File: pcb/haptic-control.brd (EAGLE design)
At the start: 40 x 160 mm, 148 parts, among them M1 SPH0641LM4H-1, P1 2P-PAD_1X3.5, P2 2P-PAD_1X3.5, P3 2P-PAD_1X3.5, P4 2P-PAD_1X3.5, U1 MIC23159, U10 DRV2605L, U11 DRV2605L, U12 MTCH6301, U2 BQ51050B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

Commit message: Nothing to do Needs revision
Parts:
- moved C52 31.9 mm to (14.2, 44.9), turned to 90 degrees
- moved R32 31.9 mm to (13.0, 44.9), turned to 270 degrees
- moved C51 27.0 mm to (9.70, 67.0)
- moved R30 27.0 mm to (9.70, 65.7)
- moved C56 22.4 mm to (30.1, 46.0), turned to 180 degrees
- moved R36 19.9 mm to (30.1, 47.2), turned to 0 degrees
- moved JP3 16.6 mm to (33.3, 42.4)
- moved JP1 16.5 mm to (37.0, 24.4), turned to 180 degrees
- moved JP2 14.5 mm to (37.0, 27.2), turned to 180 degrees
- moved C25 14.2 mm to (30.2, 42.4), turned to 90 degrees
- moved R20 13.4 mm to (31.5, 42.4), turned to 90 degrees
- moved C55 10.5 mm to (27.9, 63.8), turned to 180 degrees
- moved R34 8.29 mm to (27.9, 65.0), turned to 0 degrees
- moved C10 6.01 mm to (11.7, 35.3), turned to 270 degrees
- moved C32 4.32 mm to (26.1, 30.4)
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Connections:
- net FSR_CH_N renamed FSR_2
- removed net FSR_CH_P: C51.1, R29.1, R30.2, U5.39
- removed net FSR_VOL_N: C56.1, R35.2, R36.2, U5.37
- removed net FSR_VOL_P: C55.1, R33.2, R34.2, U5.40
- new net FSR_1: C51.1, R29.1, R30.2, U5.37
- new net FSR_3: C55.1, R33.2, R34.2, U5.39
- new net FSR_4: C56.1, R35.2, R36.2, U5.40
- net !QI_CHG: now also U5.19; no longer U5.18
- net 1V8_PG: now also U5.41; no longer U5.20
- net I2S_CLK: now also U5.31; no longer U5.30
- net I2S_DATIN: now also U5.30; no longer U5.29
- net LRA_EN: now also U5.14; no longer U5.6
- net MPU_INT: now also U5.32; no longer U5.28
- net QI_CTRL: now also U5.18; no longer U5.19
- net SCL: no longer R23.1
- net SDA: now also R23.1
- net TC_!RESET: now also U5.28; no longer U5.31
- net TC_INT: now also U5.29; no longer U5.32
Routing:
- net 3.3V: track 8.72 -> 275.6 mm, vias 0 -> 12
- net VBAT: track 91.9 -> 226.1 mm, vias 1 -> 8
- net SCL: track 81.7 -> 189.2 mm, vias 0 -> 7
- net SDA: track 82.4 -> 188.2 mm, vias 0 -> 5
- net LRA_EN: track 82.8 -> 164.4 mm, vias 0 -> 4
- net TC_!RESET: track 2.33 -> 72.1 mm, vias 0 -> 6
- net VDDS: track 0.00 -> 66.5 mm, vias 0 -> 7
- net TC_INT: track 0.00 -> 65.9 mm, vias 0 -> 6
- net MPU_INT: track 0.00 -> 54.2 mm, vias 0 -> 4
- net FSR_1: track 0.00 -> 51.1 mm, vias 0 -> 4
- net 1.8V: track 0.00 -> 48.8 mm, vias 0 -> 4
- net FSR_3: track 0.00 -> 44.6 mm, vias 0 -> 4
- net 1V8_PG: track 0.00 -> 39.7 mm, vias 0 -> 4
- net VBAT_SNS: track 0.00 -> 36.5 mm, vias 0 -> 4
- net MCU_!RESET: track 0.00 -> 36.3 mm, vias 0 -> 5
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
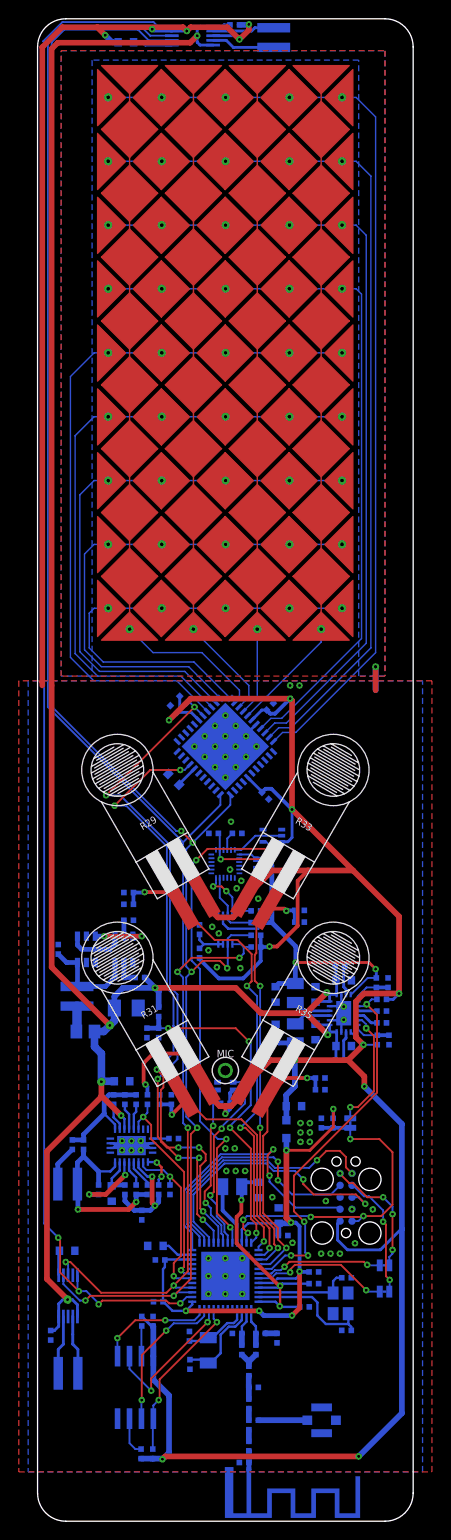
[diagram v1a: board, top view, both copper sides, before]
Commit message: minor routing changes
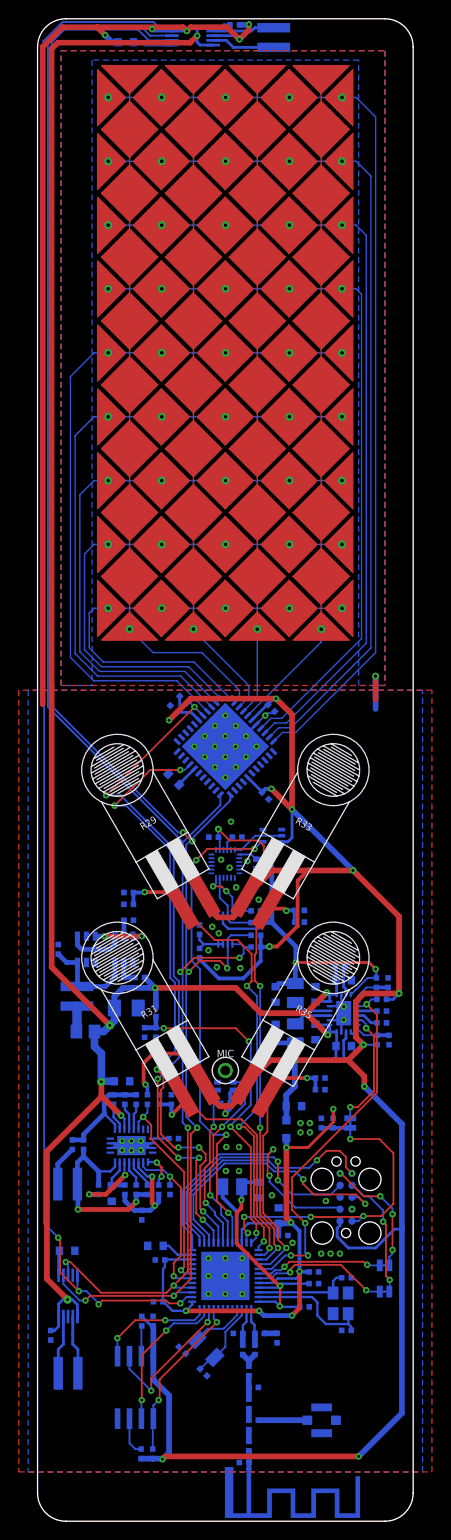
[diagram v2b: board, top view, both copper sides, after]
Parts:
- moved C43 1.68 mm to (17.7, 15.8), turned to 225 degrees
- moved C42 1.68 mm to (15.4, 18.2), turned to 45 degrees
- moved C45 0.40 mm to (21.2, 72.8)
- moved C46 0.40 mm to (18.8, 72.8)
- moved X2 0.32 mm to (17.9, 18.4), turned to 225 degrees
- moved R16 0.30 mm to (12.6, 52.0)
- moved R15 0.30 mm to (12.6, 54.2)
- moved C18 0.25 mm to (11.4, 52.0)
- moved C58 0.21 mm to (24.9, 86.6), turned to 225 degrees
- moved C33 0.10 mm to (23.1, 18.2)
- moved C34 0.10 mm to (21.4, 20.0)
- moved L6 0.10 mm to (21.9, 18.2)
- moved L7 0.10 mm to (23.6, 20.0)
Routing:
- net GND: track 123.7 -> 129.2 mm, vias 70 -> 65
- net 3.3V: track 275.6 -> 272.5 mm, vias 12 -> 14
- net MPU_INT: track 54.2 -> 52.3 mm
- net 1.8V: track 48.8 -> 50.3 mm
- net XTAL_32K_Q1: track 9.90 -> 8.41 mm
- net VDDS: track 66.5 -> 65.8 mm
- net SDA: track 188.2 -> 187.7 mm

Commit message: finished routing
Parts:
- added C62: 10u, Passive Components > Capacitors > Multilayer Ceramic Capacitors MLCC:0603_WAVE
- moved U$3 67.4 mm to (3.00, 75.0)
- moved LOGO1 27.6 mm to (29.5, 72.0)
- moved C39 0.61 mm to (13.2, 29.2)
- moved C28 0.50 mm to (13.6, 27.8)
- moved C44 0.34 mm to (32.6, 25.8)
- moved C41 0.30 mm to (32.6, 20.3)
- moved C27 0.20 mm to (13.1, 23.4)
- moved C48 0.15 mm to (17.4, 63.0)
- moved R28 0.15 mm to (17.4, 60.5)
- moved P4 0.05 mm to (25.1, 158.1)
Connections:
- net GND: now also C62.P$2
- net VBAT: now also C62.P$1
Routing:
- net 3.3V: track 272.5 -> 260.2 mm
- net VBAT: track 226.0 -> 229.8 mm, vias 8 -> 9
- net JTAG_TDI: track 29.3 -> 25.6 mm
- net GND: track 129.2 -> 131.0 mm, vias 65 -> 252
- net FSR_1: track 51.2 -> 50.3 mm
- net I2S_DATIN: track 17.6 -> 18.5 mm
- net LRA_EN: track 164.4 -> 165.1 mm
- net N$21: track 6.21 -> 5.56 mm
- net N$2: track 3.49 -> 2.85 mm
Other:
- outline, holes or cut-outs redrawn
- board text added: "CC2642R"

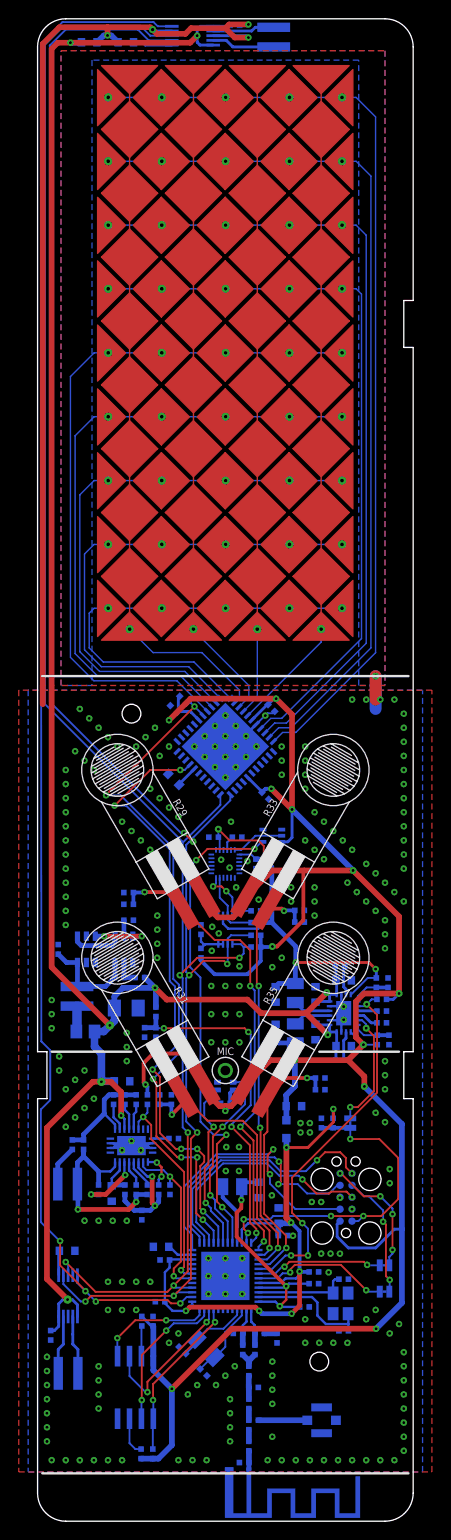
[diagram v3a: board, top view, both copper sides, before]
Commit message: changed component values, created bom, changed bat prot ic
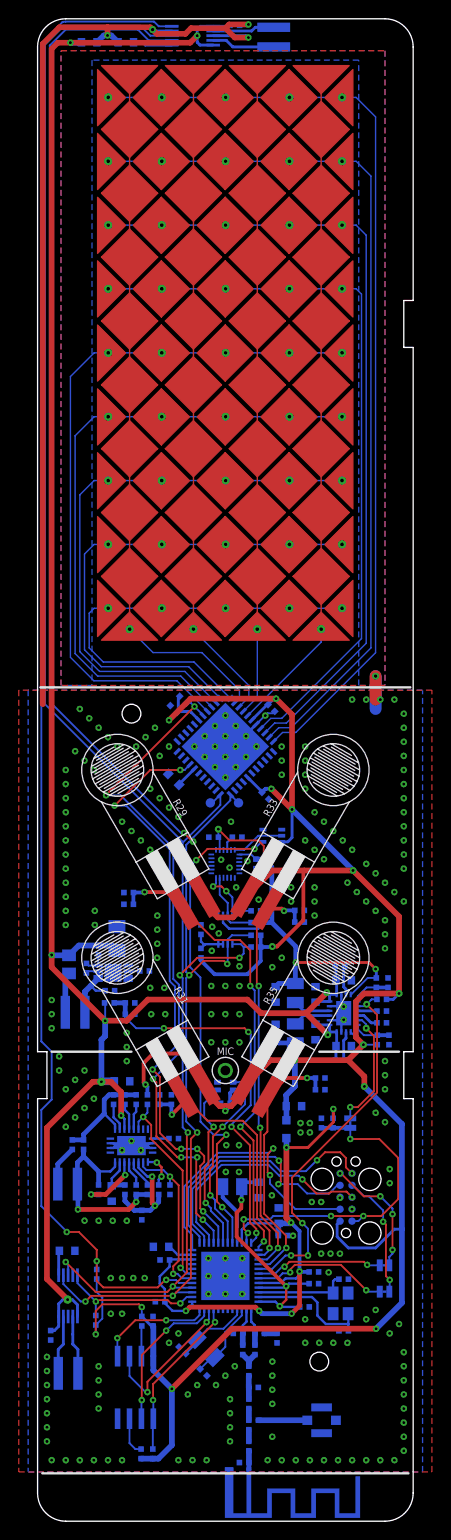
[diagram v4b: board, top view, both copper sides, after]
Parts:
- removed U4: FS8205, Fortune:SOT23-6
- added R1, R38: 100k, Passive Components > Resistors > Chip Resistors:_0402
- added SCL, SDA: TEST_POINT, Utility > Board:TEST_POINT
- C14, C15, C17, C19, C2, C4: value 4u7 -> 10u
- L4, L5: value 2N -> 2n
- R16: value 49.9k -> 49k9
- R17: value 100 -> 330
- R18: value 1k -> 2k7
- R3: value 71.5k -> 71k5
- R30, R32, R34, R36: value 3.4k -> 3k4
- U3: value FS312F-G -> AP9211; device Fortune:SOT23-6 -> Power > Battery Management:DFN2030-6
- moved C21 7.47 mm to (8.45, 62.0), turned to 90 degrees
- moved F1 7.36 mm to (3.35, 59.3), turned to 90 degrees
- moved R19 7.04 mm to (7.70, 56.5), turned to 180 degrees
- moved R18 5.66 mm to (11.4, 58.6)
- moved R17 5.27 mm to (6.50, 60.8), turned to 90 degrees
- moved R15 5.04 mm to (7.65, 55.2), turned to 0 degrees
- moved R16 4.18 mm to (9.85, 55.2), turned to 0 degrees
- moved C20 3.64 mm to (5.20, 58.9), turned to 270 degrees
- moved U3 2.75 mm to (8.05, 58.4), turned to 180 degrees
- moved C18 2.49 mm to (9.85, 54.0), turned to 180 degrees
- moved P2 1.71 mm to (4.00, 54.2), turned to 0 degrees
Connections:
- removed net LRA_EN: U10.5, U11.5, U5.14
- removed net N$24: R18.2, U3.2
- removed net N$38: F1.1, P2.1
- removed net PCAP_RX10: U12.14
- removed net PCAP_RX11: U12.11
- removed net PCAP_RX12: U12.10
- removed net PCAP_RX9: U12.15
- removed net PCAP_TX10: U12.42
- removed net PCAP_TX11: U12.43
- removed net PCAP_TX12: U12.13
- removed net PCAP_TX13: U12.12
- removed net PCAP_TX14: U12.5
- removed net PCAP_TX15: U12.4
- removed net PCAP_TX16: U12.3
- removed net PCAP_TX17: U12.2
- removed net PCAP_TX4: U12.34
- removed net PCAP_TX5: U12.38
- removed net PCAP_TX6: U12.37
- removed net PCAP_TX7: U12.36
- removed net PCAP_TX8: U12.35
- removed net PCAP_TX9: U12.41
- new net LRA1_EN: R1.1, U10.5, U5.14
- new net LRA2_EN: R38.1, U11.5, U5.17
- net 3.3V: now also R1.2, R38.2
- net GBAT: now also P2.1, R19.1, U3.1, U3.2; no longer P2.2, R19.2, U3.6, U4.3
- net GND: now also R19.2, U3.6; no longer R19.1, U4.1
- net N$21: now also R18.2, U3.5; no longer U3.1, U4.4
- net N$22: now also F1.1, P2.2; no longer U3.3, U4.6
- net N$23: now also U3.3; no longer U3.5
- net SCL: now also SCL.1
- net SDA: now also SDA.1
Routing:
- net LRA_EN: track 165.1 -> 0.00 mm, vias 4 -> 0
- net LRA2_EN: track 0.00 -> 162.8 mm, vias 0 -> 3
- net LRA1_EN: track 0.00 -> 15.9 mm, vias 0 -> 2
- net 3.3V: track 260.2 -> 275.4 mm, vias 14 -> 16
- net N$21: track 5.56 -> 1.25 mm
- net VBAT_SNS: track 37.1 -> 41.3 mm
- net GBAT: track 11.0 -> 8.02 mm
- net N$38: track 2.73 -> 0.00 mm
- net VBAT: track 229.8 -> 231.8 mm
- net N$24: track 1.70 -> 0.00 mm
- net N$22: track 5.90 -> 4.30 mm, vias 2 -> 0
- net SDA: track 188.1 -> 189.6 mm
- net SCL: track 189.0 -> 190.2 mm
- net GND: vias 252 -> 251
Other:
- board text added: "R3"

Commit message: finished bom, exported gerbers
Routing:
- net VBAT: track 231.8 -> 231.2 mm
- net GND: vias 251 -> 259
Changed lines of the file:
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@@
 <?xml version="1.0" encoding="utf-8"?>
 <!DOCTYPE eagle SYSTEM "eagle.dtd">
-<eagle version="9.3.0">
+<eagle version="9.3.2">
 <drawing>
 <settings>
-<setting alwaysvectorfont="no"/>
+<setting alwaysvectorfont="yes"/>
 <setting verticaltext="up"/>
 </settings>
@@
 </element>
 <element name="R19" library="Passive Components &gt; Resistors &gt; Chip Resistors" package="_0402" value="10M" x="7.7" y="56.5" smashed="yes" rot="MR180">
-<attribute name="NAME" x="7.6475" y="55.4061" size="0.8" layer="26" font="vector" ratio="12" rot="MR180" align="center"/>
+<attribute name="NAME" x="9.8475" y="56.5061" size="0.8" layer="26" font="vector" ratio="12" rot="MR180" align="center"/>
 </element>
 <element name="C20" library="Passive Components &gt; Capacitors &gt; Multilayer Ceramic Capacitors MLCC" package="_0402" value="100n" x="5.2" y="58.9" smashed="yes" rot="MR270">
-<attribute name="NAME" x="6.3061" y="58.8525" size="0.8" layer="26" font="vector" ratio="12" rot="MR270" align="center"/>
+<attribute name="NAME" x="5.2061" y="61.0525" size="0.8" layer="26" font="vector" ratio="12" rot="MR270" align="center"/>
 </element>
 <element name="R17" library="Passive Components &gt; Resistors &gt; Chip Resistors" package="_0402" value="330" x="6.5" y="60.8" smashed="yes" rot="MR90">
-<attribute name="NAME" x="7.5939" y="60.8475" size="0.8" layer="26" font="vector" ratio="12" rot="MR90" align="center"/>
+<attribute name="NAME" x="6.4939" y="62.9475" size="0.8" layer="26" font="vector" ratio="12" rot="MR90" align="center"/>
 </element>
 <element name="R15" library="Passive Components &gt; Resistors &gt; Chip Resistors" package="_0402" value="100k" x="7.65" y="55.2" smashed="yes" rot="MR0">
-<attribute name="NAME" x="7.6025" y="56.3939" size="0.8" layer="26" font="vector" ratio="12" rot="MR0" align="center"/>
+<attribute name="NAME" x="7.6025" y="53.9939" size="0.8" layer="26" font="vector" ratio="12" rot="MR0" align="center"/>
 </element>
 <element name="R16" library="Passive Components &gt; Resistors &gt; Chip Resistors" package="_0402" value="49k9" x="9.85" y="55.2" smashed="yes" rot="MR0">
-<attribute name="NAME" x="9.8025" y="56.3939" size="0.8" layer="26" font="vector" ratio="12" rot="MR0" align="center"/>
+<attribute name="NAME" x="12.1025" y="55.1939" size="0.8" layer="26" font="vector" ratio="12" rot="MR0" align="center"/>
 </element>
 <element name="C18" library="Passive Components &gt; Capacitors &gt; Multilayer Ceramic Capacitors MLCC" package="_0402" value="470p" x="9.85" y="54" smashed="yes" rot="MR180">
-<attribute name="NAME" x="9.8975" y="52.8061" size="0.8" layer="26" font="vector" ratio="12" rot="MR180" align="center"/>
+<attribute name="NAME" x="12.1975" y="54.0061" size="0.8" layer="26" font="vector" ratio="12" rot="MR180" align="center"/>
 </element>
 <element name="R18" library="Passive Components &gt; Resistors &gt; Chip Resistors" package="_0402" value="2k7" x="11.4" y="58.6" smashed="yes" rot="MR0">
-<attribute name="NAME" x="11.4525" y="59.6939" size="0.8" layer="26" font="vector" ratio="12" rot="MR0" align="center"/>
+<attribute name="NAME" x="13.6525" y="58.5939" size="0.8" layer="26" font="vector" ratio="12" rot="MR0" align="center"/>
 </element>
 <element name="P2" library="Connectors &gt; Other" package="PAD1X3_5MM-2P" value="2P-PAD_1X3.5" x="4" y="54.2" smashed="yes" rot="MR0">
-<attribute name="NAME" x="2.96" y="56.816" size="0.8" layer="26" font="vector" ratio="12" rot="MR0" align="center"/>
+<attribute name="NAME" x="5.16" y="56.816" size="0.8" layer="26" font="vector" ratio="12" rot="MR0" align="center"/>
 </element>
 <element name="P1" library="Connectors &gt; Other" package="PAD1X3_5MM-2P" value="2P-PAD_1X3.5" x="3.2" y="35.9" smashed="yes" rot="MR180">
@@
 </element>
 <element name="C21" library="Passive Components &gt; Capacitors &gt; Multilayer Ceramic Capacitors MLCC" package="_1206" value="100u" x="8.45" y="62.05" smashed="yes" rot="MR90">
-<attribute name="NAME" x="10.2613" y="60.8275" size="0.8" layer="26" font="vector" ratio="12" rot="MR90" align="center"/>
+<attribute name="NAME" x="10.1613" y="63.3275" size="0.8" layer="26" font="vector" ratio="12" rot="MR90" align="center"/>
 </element>
 <element name="U$1" library="Eletromechanical &gt; LRAs" package="G0825001" value="" x="5" y="5" smashed="yes" rot="MR170"/>
@@
 </element>
 <element name="F1" library="PTC Fuses" package="0805" value="500mA" x="3.35" y="59.3" smashed="yes" rot="MR90">
-<attribute name="NAME" x="5.0212" y="60.5068" size="0.8" layer="26" font="vector" ratio="12" rot="SMR270" align="center"/>
+<attribute name="NAME" x="3.8068" y="61.8788" size="0.8" layer="26" font="vector" ratio="12" rot="SMR0" align="center"/>
 <attribute name="VALUE" x="-0.2124" y="55.7694" size="0.8" layer="28" font="vector" ratio="12" rot="SMR90" align="center"/>
 </element>
@@
 </element>
 <element name="U3" library="Power &gt; Battery Management" package="DFN2030-6" value="AP9211" x="8.05" y="58.4" smashed="yes" rot="MR180">
-<attribute name="NAME" x="8.15" y="56.495" size="0.8" layer="26" font="vector" ratio="12" rot="MR180" align="center"/>
+<attribute name="NAME" x="10.65" y="59.995" size="0.8" layer="26" font="vector" ratio="12" rot="MR180" align="center"/>
 </element>
 </elements>
@@
 <contactref element="U3" pad="6"/>
 <contactref element="R18" pad="1"/>
+<via x="12.1" y="53.9" extent="1-16" drill="0.3" diameter="0.6"/>
+<via x="13.6" y="53.9" extent="1-16" drill="0.3" diameter="0.6"/>
+<via x="12" y="56.8" extent="1-16" drill="0.3" diameter="0.6"/>
+<via x="13.5" y="56.8" extent="1-16" drill="0.3" diameter="0.6"/>
+<via x="6.1" y="65" extent="1-16" drill="0.3" diameter="0.6"/>
+<via x="6.1" y="63.5" extent="1-16" drill="0.3" diameter="0.6"/>
+<via x="12.1" y="51.1" extent="1-16" drill="0.3" diameter="0.6"/>
+<via x="13.6" y="51.1" extent="1-16" drill="0.3" diameter="0.6"/>
 </signal>
 <signal name="XTAL_48M_N">
@@
 <wire x1="6.85" y1="46.85" x2="6.8" y2="46.8" width="0.8128" layer="16"/>
 <wire x1="6.8" y1="51.2696" x2="6.8" y2="46.8" width="0.6096" layer="16"/>
-<wire x1="7.2" y1="53.3" x2="1.5" y2="59" width="0.6096" layer="1"/>
-<wire x1="1.5" y1="59" x2="1.5" y2="60.3" width="0.6096" layer="1"/>
-<wire x1="1.5" y1="60.3" x2="1.5" y2="89" width="0.6096" layer="1"/>
+<wire x1="7.2" y1="53.3" x2="2.1" y2="58.4" width="0.6096" layer="1"/>
+<wire x1="2.1" y1="58.4" x2="2.1" y2="60.3" width="0.6096" layer="1"/>
+<wire x1="1.5" y1="62.8" x2="1.5" y2="89" width="0.6096" layer="1"/>
 <wire x1="6.8" y1="46.8" x2="5.9" y2="46.8" width="0.6096" layer="1"/>
 <wire x1="5.9" y1="46.8" x2="1" y2="41.9" width="0.6096" layer="1"/>
@@
 <wire x1="6.5" y1="61.308" x2="7.922" y2="61.308" width="0.6096" layer="16"/>
 <wire x1="7.922" y1="61.308" x2="8.45" y2="60.78" width="0.6096" layer="16"/>
-<wire x1="3.35" y1="60.2652" x2="1.5348" y2="60.2652" width="0.6096" layer="16"/>
-<wire x1="1.5348" y1="60.2652" x2="1.5" y2="60.3" width="0.6096" layer="16"/>
-<via x="1.5" y="60.3" extent="1-16" drill="0.3"/>
 <wire x1="7.2" y1="53.3" x2="7.2" y2="51.6696" width="0.6096" layer="16"/>
 <via x="7.2" y="53.3" extent="1-16" drill="0.3"/>
@@
 <wire x1="7.2" y1="53.3" x2="7.2" y2="55.142" width="0.2" layer="16"/>
 <wire x1="7.2" y1="55.142" x2="7.142" y2="55.2" width="0.2" layer="16"/>
+<wire x1="3.35" y1="60.2652" x2="2.1348" y2="60.2652" width="0.6096" layer="16"/>
+<wire x1="2.1348" y1="60.2652" x2="2.1" y2="60.3" width="0.6096" layer="16"/>
+<via x="2.1" y="60.3" extent="1-16" drill="0.35"/>
+<wire x1="2.1" y1="60.3" x2="2.1" y2="62.2" width="0.6096" layer="1"/>
+<wire x1="2.1" y1="62.2" x2="1.5" y2="62.8" width="0.6096" layer="1"/>
 </signal>
 <signal name="GBAT">
@@
 <wire x1="5.675" y1="57.025" x2="5.046" y2="56.396" width="0.6096" layer="16"/>
 <wire x1="5.046" y1="56.396" x2="5.046" y2="54.2" width="0.6096" layer="16"/>
-<wire x1="7.192" y1="56.5" x2="6.2" y2="56.5" width="0.254" layer="16"/>
-<wire x1="6.2" y1="56.5" x2="5.675" y2="57.025" width="0.254" layer="16"/>
+<wire x1="7.192" y1="56.5" x2="6.2" y2="56.5" width="0.6096" layer="16"/>
+<wire x1="6.2" y1="56.5" x2="5.675" y2="57.025" width="0.6096" layer="16"/>
 </signal>
 <signal name="N$23">
@@
 <via x="22.45" y="52.1" extent="1-16" drill="0.3"/>
 <wire x1="22.45" y1="52.1" x2="22.05" y2="52.5" width="0.2" layer="1"/>
-<wire x1="22.05" y1="52.5" x2="13.45" y2="52.5" width="0.2" layer="1"/>
-<via x="13.45" y="52.5" extent="1-16" drill="0.3"/>
+<wire x1="22.05" y1="52.5" x2="12.75" y2="52.5" width="0.2" layer="1"/>
+<via x="12.75" y="52.5" extent="1-16" drill="0.3"/>
 <wire x1="9.4" y1="55.258" x2="9.342" y2="55.2" width="0.2" layer="16"/>
 <wire x1="20.65" y1="42.25" x2="22.7" y2="44.3" width="0.2" layer="16"/>
 <wire x1="9.342" y1="54" x2="9.342" y2="53.658" width="0.2" layer="16"/>
-<wire x1="10.5" y1="52.5" x2="13.45" y2="52.5" width="0.2" layer="16"/>
+<wire x1="10.5" y1="52.5" x2="12.75" y2="52.5" width="0.2" layer="16"/>
 <wire x1="9.342" y1="53.658" x2="10.5" y2="52.5" width="0.2" layer="16"/>
 </signal>
@@
 <wire x1="2.954" y1="57.9388" x2="3.35" y2="58.3348" width="0.6096" layer="16"/>
 </signal>
-<signal name="GND1">
-<via x="12.1" y="54" extent="1-16" drill="0.3" diameter="0.6"/>
-<via x="13.6" y="54" extent="1-16" drill="0.3" diameter="0.6"/>
-</signal>
-<signal name="GND2">
-<via x="12" y="56.8" extent="1-16" drill="0.3" diameter="0.6"/>
-<via x="13.5" y="56.8" extent="1-16" drill="0.3" diameter="0.6"/>
-</signal>
-<signal name="GND3">
-<via x="6.1" y="65" extent="1-16" drill="0.3" diameter="0.6"/>
-<via x="6.1" y="63.5" extent="1-16" drill="0.3" diameter="0.6"/>
-</signal>
 </signals>
